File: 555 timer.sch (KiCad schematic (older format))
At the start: 3 parts, among them U6 U_555_timer

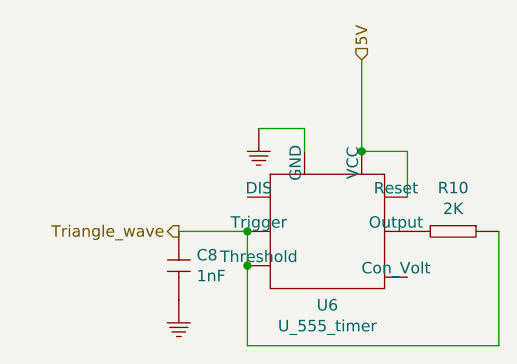
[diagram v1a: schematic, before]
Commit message: added raspberry pi hat pcb outline and layout
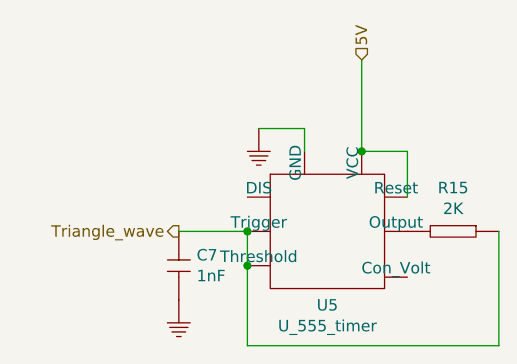
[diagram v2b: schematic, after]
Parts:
- renumbered C8 to C7, R10 to R15, U6 to U5
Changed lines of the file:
@@
 $EndDescr
 $Comp
-L Main_Library:U_555_timer U6
+L Main_Library:U_555_timer U5
 U 1 1 6158C04F
 P 5900 2900
-F 0 "U6" H 5900 2577 50  0000 C CNN
+F 0 "U5" H 5900 2577 50  0000 C CNN
 F 1 "U_555_timer" H 5900 2486 50  0000 C CNN
 F 2 "MAIN_PCB_LIB:U_LM555CN" H 5900 3400 50  0001 C CNN
@@
 Connection ~ 6050 2550
 $Comp
-L Main_Library:GND #GND021
+L Main_Library:GND #GND019
 U 1 1 6158C8C7
 P 5600 2450
-F 0 "#GND021" H 5440 2430 50  0001 C CNN
+F 0 "#GND019" H 5440 2430 50  0001 C CNN
 F 1 "GND" H 5440 2430 50  0001 C CNN
 F 2 "" H 5510 2390 50  0001 C CNN
@@
 	5800 2450 5600 2450
 $Comp
-L Main_Library:R_2K_0603 R10
+L Main_Library:R_2K_0603 R15
 U 1 1 6158D370
 P 6450 2900
-F 0 "R10" V 6260 2900 50  0000 C CNN
+F 0 "R15" V 6260 2900 50  0000 C CNN
 F 1 "R_2K_0603" H 6800 3000 50  0001 C CNN
 F 2 "MAIN_PCB_LIB:R_0603" H 6500 3400 50  0001 C CNN
@@
 Connection ~ 5550 2900
 $Comp
-L Main_Library:C_1nF_0603_50V C8
+L Main_Library:C_1nF_0603_50V C7
 U 1 1 61590D9D
 P 5250 3050
-F 0 "C8" H 5328 3096 50  0000 L CNN
+F 0 "C7" H 5328 3096 50  0000 L CNN
 F 1 "C_1nF_0603_50V" H 5300 3400 50  0001 C CNN
 F 2 "MAIN_PCB_LIB:C_0603" H 5300 3400 50  0001 C CNN
@@
 $EndComp
 $Comp
-L Main_Library:GND #GND020
+L Main_Library:GND #GND018
 U 1 1 61591AE3
 P 5250 3200
-F 0 "#GND020" H 5090 3180 50  0001 C CNN
+F 0 "#GND018" H 5090 3180 50  0001 C CNN
 F 1 "GND" H 5090 3180 50  0001 C CNN
 F 2 "" H 5160 3140 50  0001 C CNN

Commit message: changed everything to 9V and changed inductor to match one in stock
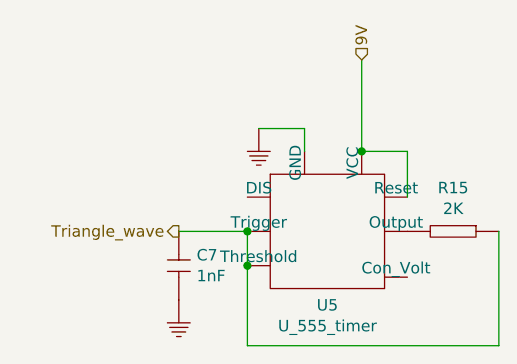
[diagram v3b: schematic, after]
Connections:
- net 5V renamed 9V
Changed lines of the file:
@@
 $Descr A4 11693 8268
 encoding utf-8
-Sheet 4 5
+Sheet 3 4
 Title ""
 Date ""
@@
 	1    0    0    -1
 $EndComp
-Text HLabel 6050 2150 1    50   Input ~ 0
-5V
 Wire Wire Line
 	6050 2150 6050 2550
@@
 Text HLabel 5250 2900 0    50   Output ~ 0
 Triangle_wave
+Text HLabel 6050 2150 1    50   Input ~ 0
+9V
 $EndSCHEMATC
